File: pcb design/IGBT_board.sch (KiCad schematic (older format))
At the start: 64 parts, among them J1 4-794627-0, Q1 IGBT, Q10 IGBT, Q11 IGBT, Q12 IGBT, Q2 IGBT, Q3 IGBT, Q4 IGBT, Q5 IGBT, Q6 IGBT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

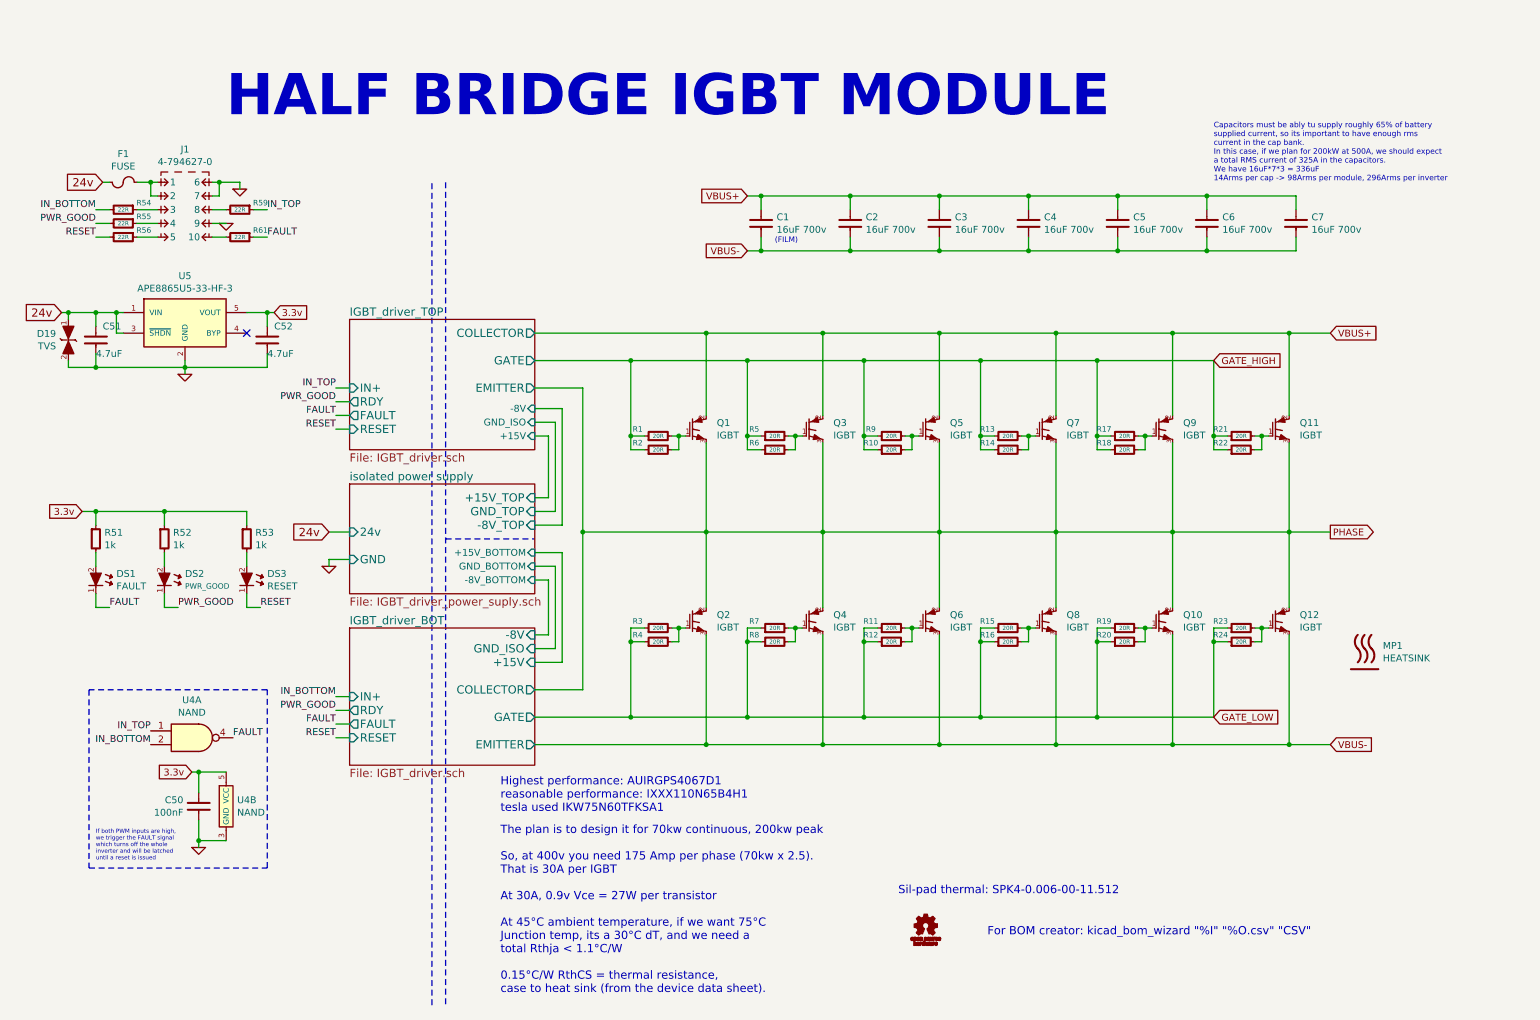
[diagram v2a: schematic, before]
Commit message: Added gate voltage control, more decoupling pads for the buffer transistors, added notes
Signed-off-by: Marcos Chaparro <mchaparro@paltatech.com>
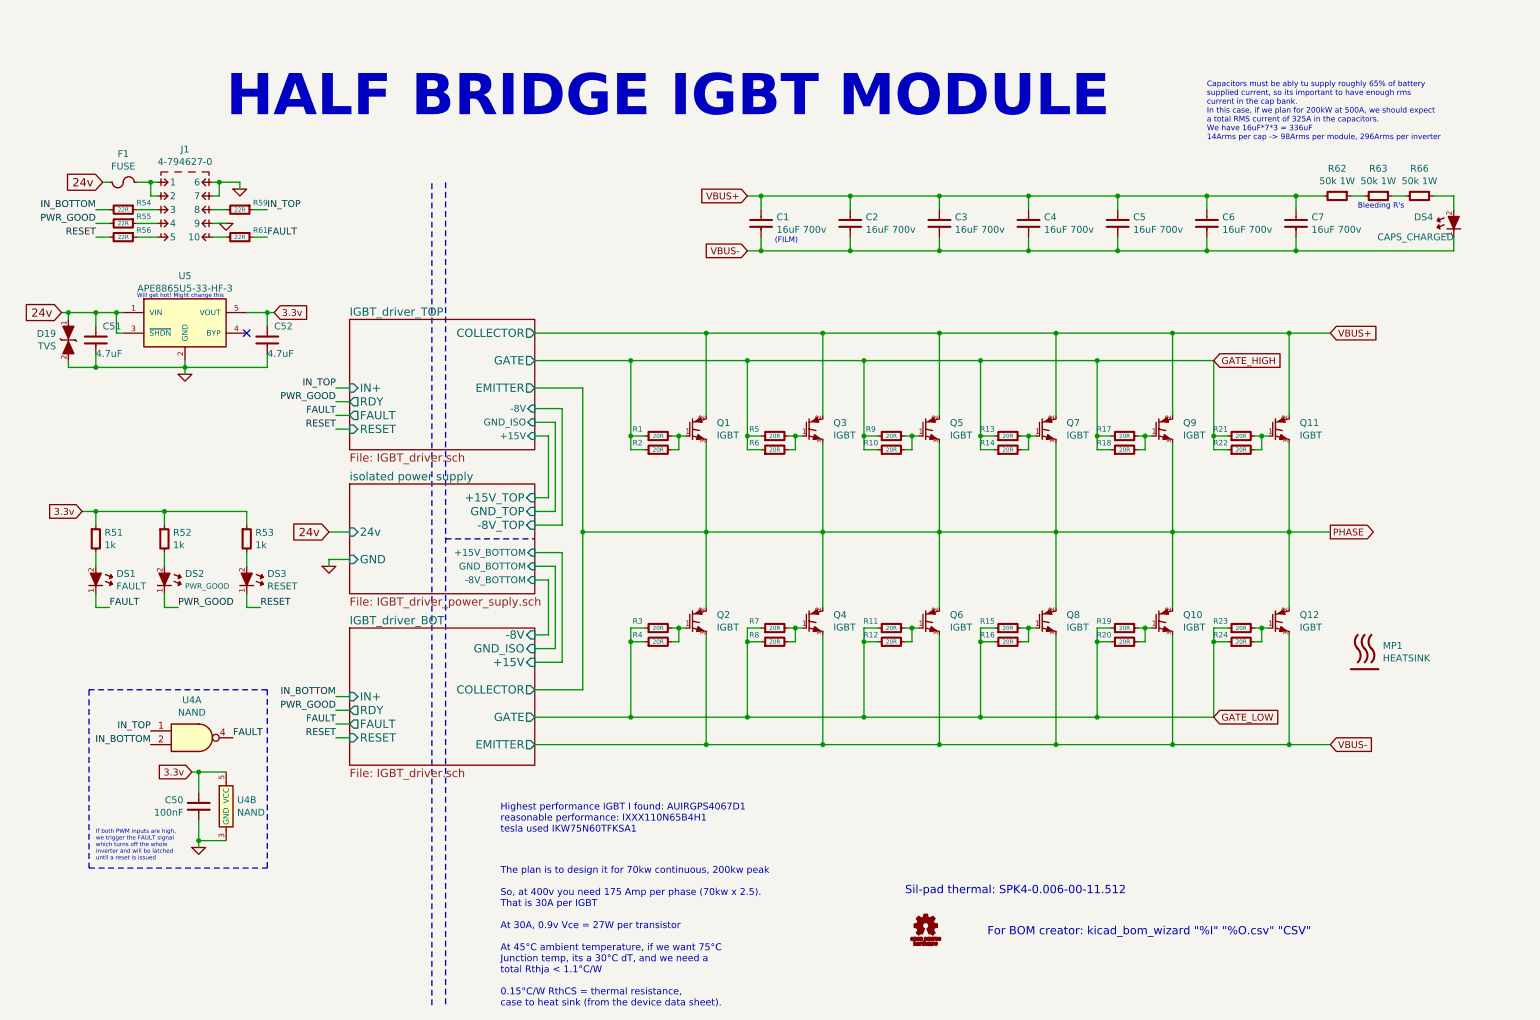
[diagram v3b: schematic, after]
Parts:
- added DS4: CAPS_CHARGED, smd-semi:LED-0603, symbol LED-0603
- added R62, R63, R66: 50k 1W, IPC7351-Nominal:RESC6432X70, symbol R-2512
- C1, C2, C3, C4, C5, C6, C7: footprint paltatech:CAP_FILM_EPCOS_42x20mm -> paltatech:CAP_FILM_EPCOS_42x20mm_3D_only
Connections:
- net VBUS+: now also R62.2
- net VBUS-: now also DS4.1 (K)
- new net: R62.1, R63.2
- new net: R63.1, R66.2
- new net: DS4.2 (A), R66.1
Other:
- note added: "Bleeding R's"
- note added: "Highest performance IGBT I found: AUIRGPS4067D1\nreasonable performance: IXXX110N65B4H1\ntesla used IKW75N60TFKSA1"
- note added: "Will get hot! Might change this"
- note removed: "Highest performance: AUIRGPS4067D1\nreasonable performance: IXXX110N65B4H1\ntesla used IKW75N60TFKSA1"
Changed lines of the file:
@@
 $Descr A4 11693 8268
 encoding utf-8
-Sheet 1 4
+Sheet 1 6
 Title "IGBT module"
 Date "2016-11-24"
@@
 	1    0    0    -1
 $EndComp
-Text Notes 4050 6350 0    60   ~ 0
-Highest performance: AUIRGPS4067D1\nreasonable performance: IXXX110N65B4H1\ntesla used IKW75N60TFKSA1
+Text Notes 4050 6500 0    50   ~ 0
+Highest performance IGBT I found: AUIRGPS4067D1\nreasonable performance: IXXX110N65B4H1\ntesla used IKW75N60TFKSA1
 $Comp
 L R-2512 R1
@@
 F 0 "C1" H 6063 2096 50  0000 L CNN
 F 1 "16uF 700v" H 6063 2005 50  0000 L CNN
-F 2 "paltatech:CAP_FILM_EPCOS_42x20mm" H 5950 2050 50  0001 C CNN
+F 2 "paltatech:CAP_FILM_EPCOS_42x20mm_3D_only" H 5950 2050 50  0001 C CNN
 F 3 "" H 5940 2025 60  0000 C CNN
 F 4 "B32796G3166K" H 5950 2050 60  0001 C CNN "mfg#"
@@
 F 0 "C2" H 6713 2096 50  0000 L CNN
 F 1 "16uF 700v" H 6713 2005 50  0000 L CNN
-F 2 "paltatech:CAP_FILM_EPCOS_42x20mm" H 6600 2050 50  0001 C CNN
+F 2 "paltatech:CAP_FILM_EPCOS_42x20mm_3D_only" H 6600 2050 50  0001 C CNN
 F 3 "" H 6590 2025 60  0000 C CNN
 F 4 "B32796G3166K" H 6600 2050 60  0001 C CNN "mfg#"
@@
 F 0 "C3" H 7363 2096 50  0000 L CNN
 F 1 "16uF 700v" H 7363 2005 50  0000 L CNN
-F 2 "paltatech:CAP_FILM_EPCOS_42x20mm" H 7250 2050 50  0001 C CNN
+F 2 "paltatech:CAP_FILM_EPCOS_42x20mm_3D_only" H 7250 2050 50  0001 C CNN
 F 3 "" H 7240 2025 60  0000 C CNN
 F 4 "B32796G3166K" H 7250 2050 60  0001 C CNN "mfg#"
@@
 F 0 "C4" H 8013 2096 50  0000 L CNN
 F 1 "16uF 700v" H 8013 2005 50  0000 L CNN
-F 2 "paltatech:CAP_FILM_EPCOS_42x20mm" H 7900 2050 50  0001 C CNN
+F 2 "paltatech:CAP_FILM_EPCOS_42x20mm_3D_only" H 7900 2050 50  0001 C CNN
 F 3 "" H 7890 2025 60  0000 C CNN
 F 4 "B32796G3166K" H 7900 2050 60  0001 C CNN "mfg#"
@@
 F 0 "C5" H 8663 2096 50  0000 L CNN
 F 1 "16uF 700v" H 8663 2005 50  0000 L CNN
-F 2 "paltatech:CAP_FILM_EPCOS_42x20mm" H 8550 2050 50  0001 C CNN
+F 2 "paltatech:CAP_FILM_EPCOS_42x20mm_3D_only" H 8550 2050 50  0001 C CNN
 F 3 "" H 8540 2025 60  0000 C CNN
 F 4 "B32796G3166K" H 8550 2050 60  0001 C CNN "mfg#"
@@
 F 0 "C6" H 9313 2096 50  0000 L CNN
 F 1 "16uF 700v" H 9313 2005 50  0000 L CNN
-F 2 "paltatech:CAP_FILM_EPCOS_42x20mm" H 9200 2050 50  0001 C CNN
+F 2 "paltatech:CAP_FILM_EPCOS_42x20mm_3D_only" H 9200 2050 50  0001 C CNN
 F 3 "" H 9190 2025 60  0000 C CNN
 F 4 "B32796G3166K" H 9200 2050 60  0001 C CNN "mfg#"
@@
 F 0 "C7" H 9963 2096 50  0000 L CNN
 F 1 "16uF 700v" H 9963 2005 50  0000 L CNN
-F 2 "paltatech:CAP_FILM_EPCOS_42x20mm" H 9850 2050 50  0001 C CNN
+F 2 "paltatech:CAP_FILM_EPCOS_42x20mm_3D_only" H 9850 2050 50  0001 C CNN
 F 3 "" H 9840 2025 60  0000 C CNN
 F 4 "B32796G3166K" H 9850 2050 60  0001 C CNN "mfg#"
@@
 	1    0    0    -1
 $EndComp
-Text Notes 4050 8250 0    60   ~ 0
+Text Notes 4050 8250 0    50   ~ 0
 The plan is to design it for 70kw continuous, 200kw peak\n\nSo, at 400v you need 175 Amp per phase (70kw x 2.5).\nThat is 30A per IGBT\n\nAt 30A, 0.9v Vce = 27W per transistor\n\nAt 45°C ambient temperature, if we want 75°C\nJunction temp, its a 30°C dT, and we need a\ntotal Rthja < 1.1°C/W\n\n0.15°C/W RthCS = thermal resistance,\ncase to heat sink (from the device data sheet). \n\n\n\n\n\n\n
-Text Notes 6950 6950 0    60   ~ 0
+Text Notes 7000 6950 0    60   ~ 0
 Sil-pad thermal: SPK4-0.006-00-11.512
-Text Notes 9250 1750 0    40   ~ 0
+Text Notes 9200 1450 0    40   ~ 0
 Capacitors must be ably tu supply roughly 65% of battery\nsupplied current, so its important to have enough rms\ncurrent in the cap bank.\nIn this case, if we plan for 200kW at 500A, we should expect\na total RMS current of 325A in the capacitors.\nWe have 16uF*7*3 = 336uF\n14Arms per cap -> 98Arms per module, 296Arms per inverter
 $Sheet
@@
 RESET
 $Comp
-L GND #PWR01
+L GND #PWR4
 U 1 1 5831A3A1
 P 2150 1800
-F 0 "#PWR01" H 2150 1800 30  0001 C CNN
+F 0 "#PWR4" H 2150 1800 30  0001 C CNN
 F 1 "GND" H 2150 1730 30  0001 C CNN
 F 2 "" H 2150 1800 60  0000 C CNN
@@
 $EndComp
 $Comp
-L GND #PWR02
+L GND #PWR5
 U 1 1 58386BF0
 P 2800 4550
-F 0 "#PWR02" H 2800 4550 30  0001 C CNN
+F 0 "#PWR5" H 2800 4550 30  0001 C CNN
 F 1 "GND" H 2800 4480 30  0001 C CNN
 F 2 "" H 2800 4550 60  0000 C CNN
@@
 $EndComp
 $Comp
-L GND #PWR03
+L GND #PWR2
 U 1 1 58387D39
 P 1850 6600
-F 0 "#PWR03" H 1850 6600 30  0001 C CNN
+F 0 "#PWR2" H 1850 6600 30  0001 C CNN
 F 1 "GND" H 1850 6530 30  0001 C CNN
 F 2 "" H 1850 6600 60  0000 C CNN
@@
 	5950 1950 5950 1850
 Wire Wire Line
-	5850 1850 9850 1850
+	5850 1850 10050 1850
 Wire Wire Line
 	6600 1850 6600 1950
@@
 Connection ~ 9200 1850
 Wire Wire Line
-	5850 2250 9850 2250
+	11000 2250 5850 2250
 Wire Wire Line
 	9850 2250 9850 2150
@@
 Connection ~ 2350 2700
 $Comp
-L GND #PWR04
+L GND #PWR1
 U 1 1 583AB791
 P 1750 3150
-F 0 "#PWR04" H 1750 3150 30  0001 C CNN
+F 0 "#PWR1" H 1750 3150 30  0001 C CNN
 F 1 "GND" H 1750 3080 30  0001 C CNN
 F 2 "" H 1750 3150 60  0000 C CNN
@@
 $EndComp
 $Comp
-L GND #PWR05
+L GND #PWR3
 U 1 1 583AF86E
 P 2050 2050
-F 0 "#PWR05" H 2050 2050 30  0001 C CNN
+F 0 "#PWR3" H 2050 2050 30  0001 C CNN
 F 1 "GND" H 2050 1980 30  0001 C CNN
 F 2 "" H 2050 2050 60  0000 C CNN
@@
 Text Label 1100 2050 2    50   ~ 0
 PWR_GOOD
+Text Notes 1400 2600 0    30   ~ 0
+Will get hot! Might change this
+$Comp
+L R-2512 R62
+U 1 1 58403845
+P 10150 1850
+F 0 "R62" V 9950 1850 50  0000 C CNN
+F 1 "50k 1W" V 10041 1850 50  0000 C CNN
+F 2 "IPC7351-Nominal:RESC6432X70" H 10150 1850 50  0001 C CNN
+F 3 "" H 10150 1900 60  0000 C CNN
+F 4 "RES SMD 1k 5% [2512]" H 10900 2400 60  0001 C CNN "BOM"
+	1    10150 1850
+	0    1    1    0
+$EndComp
+$Comp
+L R-2512 R63
+U 1 1 58404D83
+P 10450 1850
+F 0 "R63" V 10250 1850 50  0000 C CNN
+F 1 "50k 1W" V 10341 1850 50  0000 C CNN
+F 2 "IPC7351-Nominal:RESC6432X70" H 10450 1850 50  0001 C CNN
+F 3 "" H 10450 1900 60  0000 C CNN
+F 4 "RES SMD 1k 5% [2512]" H 11200 2400 60  0001 C CNN "BOM"
+	1    10450 1850
+	0    1    1    0
+$EndComp
+$Comp
+L R-2512 R66
+U 1 1 58404F13
+P 10750 1850
+F 0 "R66" V 10550 1850 50  0000 C CNN
+F 1 "50k 1W" V 10641 1850 50  0000 C CNN
+F 2 "IPC7351-Nominal:RESC6432X70" H 10750 1850 50  0001 C CNN
+F 3 "" H 10750 1900 60  0000 C CNN
+F 4 "RES SMD 1k 5% [2512]" H 11500 2400 60  0001 C CNN "BOM"
+	1    10750 1850
+	0    1    1    0
+$EndComp
+$Comp
+L LED-0603 DS4
+U 1 1 58405B3C
+P 11000 2050
+F 0 "DS4" H 11150 2096 50  0000 L CNN
+F 1 "CAPS_CHARGED" H 11000 1950 50  0000 L CNN
+F 2 "smd-semi:LED-0603" H 11000 1900 50  0001 C CNN
+F 3 "" H 11000 2050 60  0000 C CNN
+F 4 "LED RED [0603]" H 11000 1800 60  0001 C CNN "BOM"
+	1    11000 2050
+	-1   0    0    -1
+$EndComp
+Wire Wire Line
+	11000 2150 11000 2250
+Wire Wire Line
+	11000 1950 11000 1850
+Wire Wire Line
+	11000 1850 10850 1850
+Wire Wire Line
+	10650 1850 10550 1850
+Wire Wire Line
+	10350 1850 10250 1850
+Connection ~ 9850 1850
+Connection ~ 9850 2250
+Text Notes 10300 1950 0    40   ~ 0
+Bleeding R's
 $EndSCHEMATC

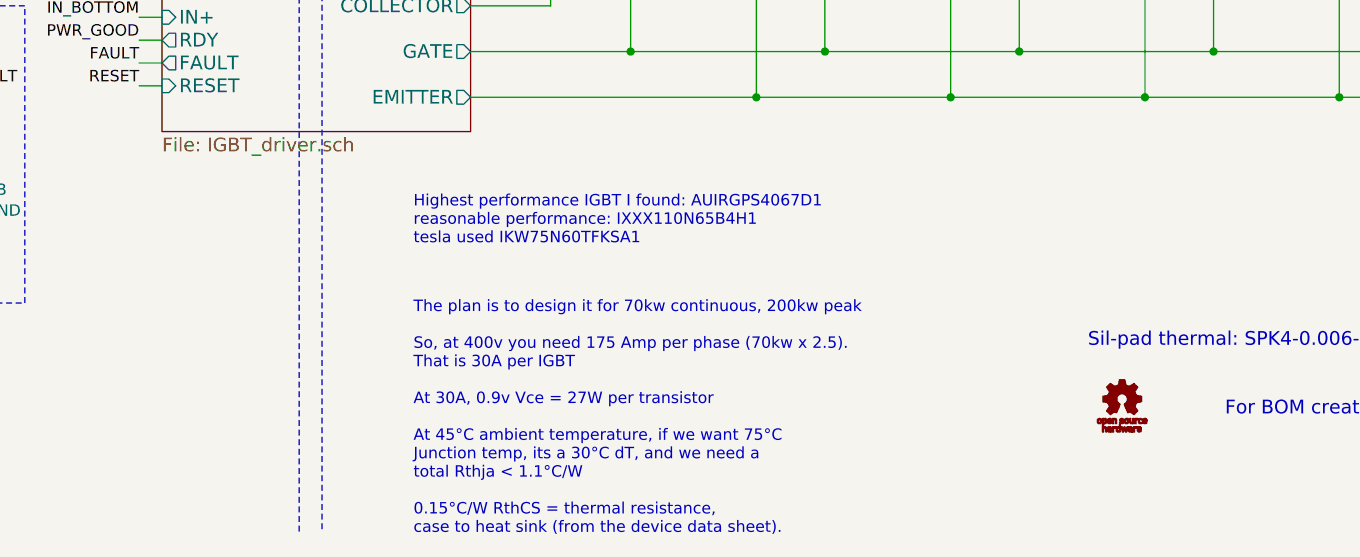
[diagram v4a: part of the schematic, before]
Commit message: Added phase voltage sensing
Signed-off-by: Marcos Chaparro <mchaparro@paltatech.com>
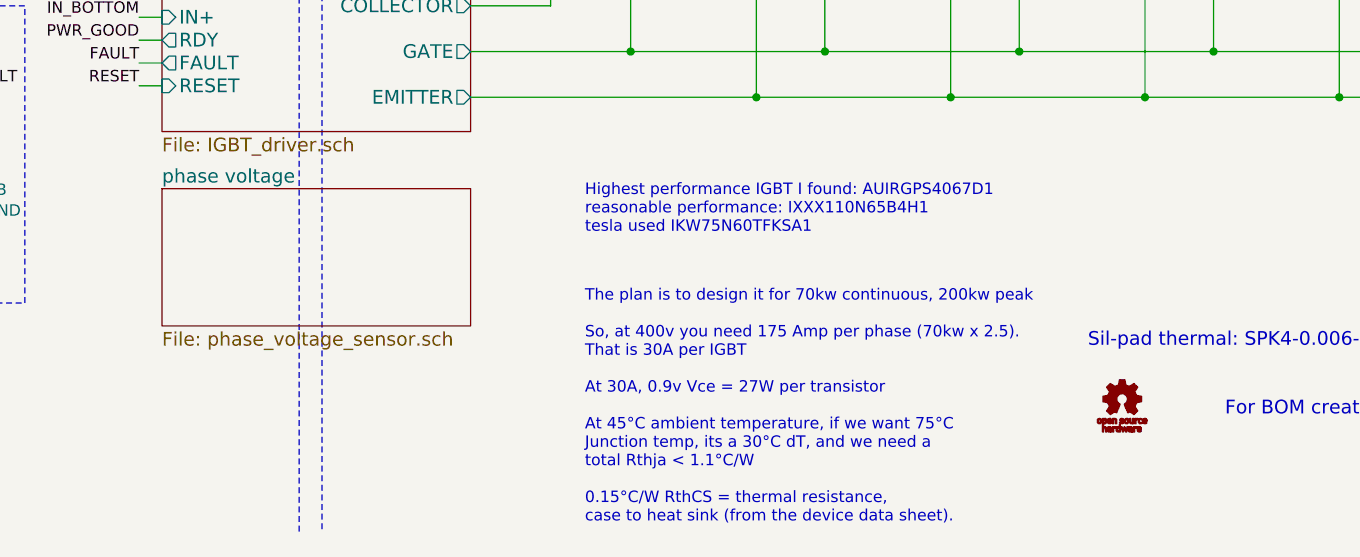
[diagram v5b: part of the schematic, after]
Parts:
- Q1, Q10, Q11, Q12, Q2, Q3, Q4, Q5, Q6, Q7, Q8, Q9: footprint pth-semi:TO-247 -> pth-semi:TO-247-HV
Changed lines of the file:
@@
 $Descr A4 11693 8268
 encoding utf-8
-Sheet 1 6
+Sheet 1 7
 Title "IGBT module"
 Date "2016-11-24"
@@
 F 0 "Q1" H 5627 3596 50  0000 L CNN
 F 1 "IGBT" H 5627 3505 50  0000 L CNN
-F 2 "pth-semi:TO-247" H 5627 3459 60  0001 L CNN
+F 2 "pth-semi:TO-247-HV" H 5627 3459 60  0001 L CNN
 F 3 "" H 5500 3600 60  0000 C CNN
 F 4 "AUIRGPS4067D1" H 5500 3550 60  0001 C CNN "mfg#"
@@
 F 0 "Q3" H 6477 3596 50  0000 L CNN
 F 1 "IGBT" H 6477 3505 50  0000 L CNN
-F 2 "pth-semi:TO-247" H 6477 3459 60  0001 L CNN
+F 2 "pth-semi:TO-247-HV" H 6477 3459 60  0001 L CNN
 F 3 "" H 6350 3600 60  0000 C CNN
 F 4 "IXXX110N65B4H1" H 6350 3550 60  0001 C CNN "mfg#"
@@
 	1    0    0    -1
 $EndComp
-Text Notes 4050 6500 0    50   ~ 0
+Text Notes 4800 6450 0    50   ~ 0
 Highest performance IGBT I found: AUIRGPS4067D1\nreasonable performance: IXXX110N65B4H1\ntesla used IKW75N60TFKSA1
 $Comp
@@
 F 0 "Q2" H 5627 4996 50  0000 L CNN
 F 1 "IGBT" H 5627 4905 50  0000 L CNN
-F 2 "pth-semi:TO-247" H 5500 5000 60  0001 C CNN
+F 2 "pth-semi:TO-247-HV" H 5500 5000 60  0001 C CNN
 F 3 "" H 5500 5000 60  0000 C CNN
 F 4 "IXXX110N65B4H1" H 5500 4950 60  0001 C CNN "mfg#"
@@
 F 0 "Q4" H 6477 4996 50  0000 L CNN
 F 1 "IGBT" H 6477 4905 50  0000 L CNN
-F 2 "pth-semi:TO-247" H 6350 5000 60  0001 C CNN
+F 2 "pth-semi:TO-247-HV" H 6350 5000 60  0001 C CNN
 F 3 "" H 6350 5000 60  0000 C CNN
 F 4 "IXXX110N65B4H1" H 6350 4950 60  0001 C CNN "mfg#"
@@
 F 0 "Q5" H 7327 3596 50  0000 L CNN
 F 1 "IGBT" H 7327 3505 50  0000 L CNN
-F 2 "pth-semi:TO-247" H 7327 3459 60  0001 L CNN
+F 2 "pth-semi:TO-247-HV" H 7327 3459 60  0001 L CNN
 F 3 "" H 7200 3600 60  0000 C CNN
 F 4 "IXXX110N65B4H1" H 7200 3550 60  0001 C CNN "mfg#"
@@
 F 0 "Q7" H 8177 3596 50  0000 L CNN
 F 1 "IGBT" H 8177 3505 50  0000 L CNN
-F 2 "pth-semi:TO-247" H 8050 3600 60  0001 C CNN
+F 2 "pth-semi:TO-247-HV" H 8050 3600 60  0001 C CNN
 F 3 "" H 8050 3600 60  0000 C CNN
 F 4 "IXXX110N65B4H1" H 8050 3550 60  0001 C CNN "mfg#"
@@
 F 0 "Q6" H 7327 4996 50  0000 L CNN
 F 1 "IGBT" H 7327 4905 50  0000 L CNN
-F 2 "pth-semi:TO-247" H 7200 5000 60  0001 C CNN
+F 2 "pth-semi:TO-247-HV" H 7200 5000 60  0001 C CNN
 F 3 "" H 7200 5000 60  0000 C CNN
 F 4 "IXXX110N65B4H1" H 7200 4950 60  0001 C CNN "mfg#"
@@
 F 0 "Q8" H 8177 4996 50  0000 L CNN
 F 1 "IGBT" H 8177 4905 50  0000 L CNN
-F 2 "pth-semi:TO-247" H 8050 5000 60  0001 C CNN
+F 2 "pth-semi:TO-247-HV" H 8050 5000 60  0001 C CNN
 F 3 "" H 8050 5000 60  0000 C CNN
 F 4 "IXXX110N65B4H1" H 8050 4950 60  0001 C CNN "mfg#"
@@
 F 0 "Q9" H 9027 3596 50  0000 L CNN
 F 1 "IGBT" H 9027 3505 50  0000 L CNN
-F 2 "pth-semi:TO-247" H 8900 3600 60  0001 C CNN
+F 2 "pth-semi:TO-247-HV" H 8900 3600 60  0001 C CNN
 F 3 "" H 8900 3600 60  0000 C CNN
 F 4 "IXXX110N65B4H1" H 8900 3550 60  0001 C CNN "mfg#"
@@
 F 0 "Q11" H 9877 3596 50  0000 L CNN
 F 1 "IGBT" H 9877 3505 50  0000 L CNN
-F 2 "pth-semi:TO-247" H 9750 3600 60  0001 C CNN
+F 2 "pth-semi:TO-247-HV" H 9750 3600 60  0001 C CNN
 F 3 "" H 9750 3600 60  0000 C CNN
 F 4 "IXXX110N65B4H1" H 9750 3550 60  0001 C CNN "mfg#"
@@
 F 0 "Q10" H 9027 4996 50  0000 L CNN
 F 1 "IGBT" H 9027 4905 50  0000 L CNN
-F 2 "pth-semi:TO-247" H 8900 5000 60  0001 C CNN
+F 2 "pth-semi:TO-247-HV" H 8900 5000 60  0001 C CNN
 F 3 "" H 8900 5000 60  0000 C CNN
 F 4 "IXXX110N65B4H1" H 8900 4950 60  0001 C CNN "mfg#"
@@
 F 0 "Q12" H 9877 4996 50  0000 L CNN
 F 1 "IGBT" H 9877 4905 50  0000 L CNN
-F 2 "pth-semi:TO-247" H 9750 5000 60  0001 C CNN
+F 2 "pth-semi:TO-247-HV" H 9750 5000 60  0001 C CNN
 F 3 "" H 9750 5000 60  0000 C CNN
 F 4 "IXXX110N65B4H1" H 9750 4950 60  0001 C CNN "mfg#"
@@
 	1    0    0    -1
 $EndComp
-Text Notes 4050 8250 0    50   ~ 0
+Text Notes 4800 8200 0    50   ~ 0
 The plan is to design it for 70kw continuous, 200kw peak\n\nSo, at 400v you need 175 Amp per phase (70kw x 2.5).\nThat is 30A per IGBT\n\nAt 30A, 0.9v Vce = 27W per transistor\n\nAt 45°C ambient temperature, if we want 75°C\nJunction temp, its a 30°C dT, and we need a\ntotal Rthja < 1.1°C/W\n\n0.15°C/W RthCS = thermal resistance,\ncase to heat sink (from the device data sheet). \n\n\n\n\n\n\n
 Text Notes 7000 6950 0    60   ~ 0
@@
 Text Notes 10300 1950 0    40   ~ 0
 Bleeding R's
+$Sheet
+S 2950 6250 1350 600
+U 585ACB8D
+F0 "phase voltage" 60
+F1 "phase_voltage_sensor.sch" 60
+$EndSheet
 $EndSCHEMATC
